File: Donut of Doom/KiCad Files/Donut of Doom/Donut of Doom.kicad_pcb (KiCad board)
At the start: 2 copper layers, 55.2 x 55.8 mm, 11 parts

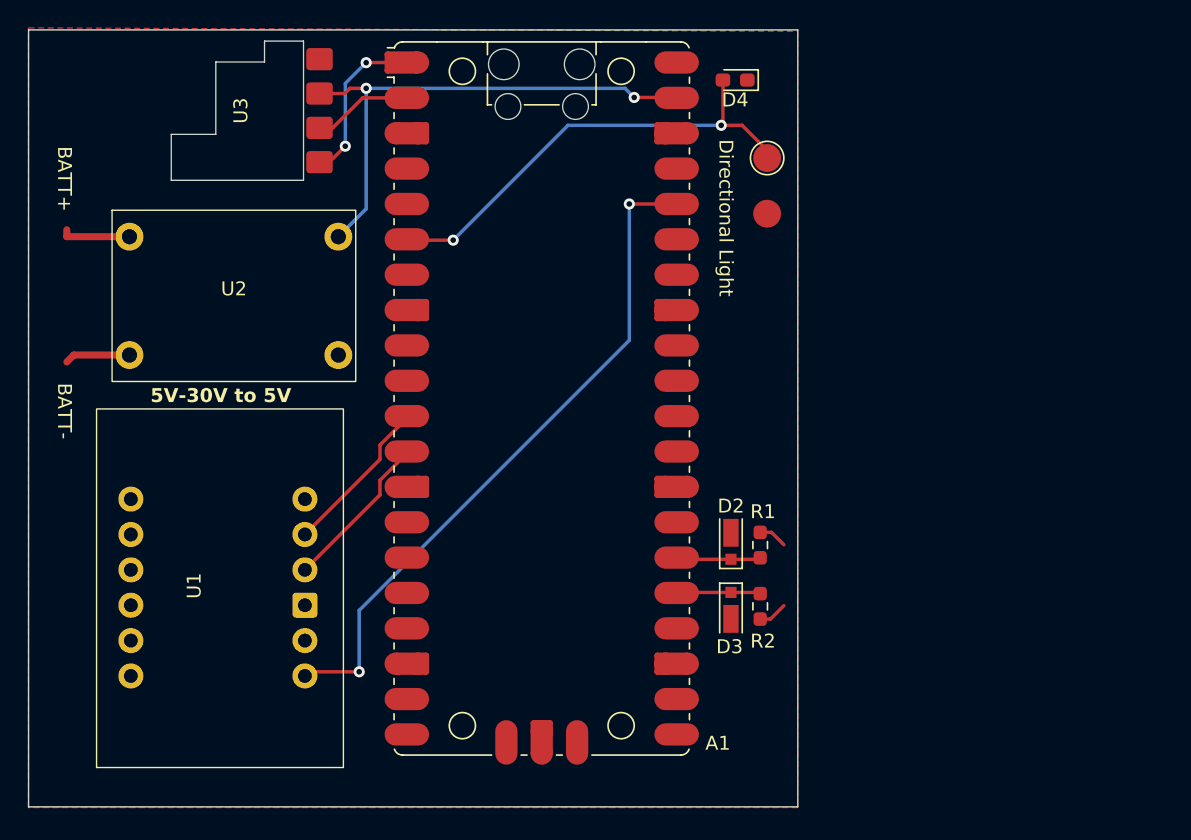
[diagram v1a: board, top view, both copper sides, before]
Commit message: New footprints for buck and accel, layout partially done.
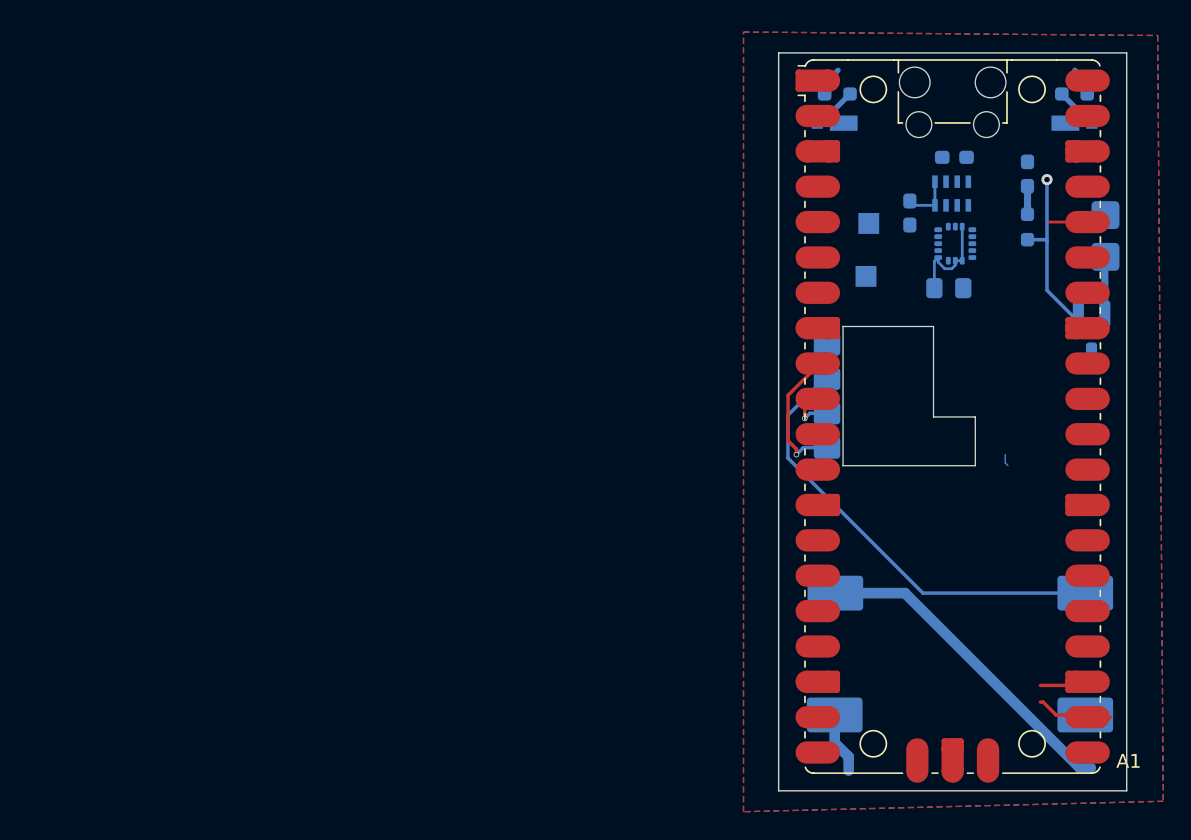
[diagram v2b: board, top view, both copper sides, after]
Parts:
- removed ?: , 
- removed the D4 at (135.0, 70.5)
- removed REF**: TestPoint_Pad_D2.0mm, TestPoint:TestPoint_Pad_D2.0mm
- removed the U1 at (91.6, 113.3)
- added 0.1uF1: 10uF, Capacitor_SMD:C_0603_1608Metric_Pad1.08x0.95mm_HandSolder, B.Cu at (147.6, 80.0)
- added C1: 10uF, Capacitor_SMD:C_0805_2012Metric_Pad1.18x1.45mm_HandSolder, B.Cu at (150.3, 85.5)
- added D1: RED 2V LED, Battlebots:2 pth Pads, B.Cu at (161.6, 81.7)
- added D2: RED 2V LED, LED_SMD:LED_0603_1608Metric_Pad1.05x0.95mm_HandSolder, B.Cu at (156.0, 77.3)
- added D6: GREEN ON LED, LED_SMD:LED_0603_1608Metric_Pad1.05x0.95mm_HandSolder, B.Cu at (150.8, 76.0)
- added Q1: Q_NMOS_GSD, Package_TO_SOT_SMD:SOT-23_Handsoldering, B.Cu at (160.6, 88.8)
- added R1: 100, Resistor_SMD:R_0603_1608Metric_Pad0.98x0.95mm_HandSolder, B.Cu at (156.0, 81.1)
- added RN1: R_Pack04_Split, Resistor_SMD:R_Array_Concave_4x0603, B.Cu at (150.6, 78.7)
- added TP1: INT1, TestPoint:TestPoint_Pad_1.5x1.5mm, B.Cu at (144.4, 84.6)
- added TP2: INT2, TestPoint:TestPoint_Pad_1.5x1.5mm, B.Cu at (144.6, 80.8)
- added U3: H3LIS331DLTR, Package_LGA:LGA-16_3x3mm_P0.5mm_LayoutBorder3x5y, B.Cu at (150.8, 82.2)
- D3, R2, U2: moved to B.Cu
- D4: renamed from D2; moved to B.Cu
- R3: renamed from R1; moved to B.Cu
- U1: renamed from U3; moved to B.Cu
- moved U2 58.1 mm to (151.2, 111.6)
- moved U1 51.0 mm to (146.8, 93.2)
- moved R3 39.5 mm to (159.4, 71.5), turned to 0 degrees
- moved D4 39.2 mm to (159.6, 73.6), turned to 180 degrees
- moved R2 37.2 mm to (142.3, 71.5), turned to 180 degrees
- moved D3 35.5 mm to (141.9, 73.6), turned to 0 degrees
- moved A1 29.5 mm to (150.6, 94.7)
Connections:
- A1 pad 1: Net-(A1-GPIO0) -> unconnected-(A1-GPIO0-Pad1)
- A1 pad 10: unconnected-(A1-GPIO7-Pad10) -> Net-(A1-GPIO7)
- A1 pad 2: Net-(A1-GPIO1) -> unconnected-(A1-GPIO1-Pad2)
- A1 pad 29: unconnected-(A1-GPIO22-Pad29) -> /Directional LED
- A1 pad 6: /GPIO4 -> unconnected-(A1-GPIO4-Pad6)
- A1 pad 9: unconnected-(A1-GPIO6-Pad9) -> Net-(A1-GPIO6)
- U1 pad 1: Net-(A1-GPIO0) -> Net-(A1-GPIO6)
- U1 pad 2: Net-(A1-GPIO1) -> Net-(A1-GPIO7)
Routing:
- net +3V3: track 48.3 -> 13.1 mm, vias 2 -> 0
- net /GPIO4: track 33.2 -> 0.00 mm, vias 2 -> 0
- net +BATT: track 5.00 -> 23.5 mm
- net Net-(A1-GPIO0): track 12.7 -> 0.00 mm, vias 2 -> 0
- net /Directional LED: track 0.00 -> 12.3 mm, vias 0 -> 1
- net /I2C0 SCL: track 12.2 -> 0.00 mm
- net /I2C0 SDA: track 12.2 -> 0.00 mm
- net Net-(A1-GPIO6): track 0.00 -> 10.6 mm, vias 0 -> 1
- net Net-(A1-GPIO1): track 7.96 -> 0.00 mm
- net unconnected-(A1-GPIO17-Pad22): track 0.00 -> 5.44 mm
- net /ESC2 PWM: track 6.89 -> 2.13 mm
- net +5V: track 36.8 -> 32.1 mm, vias 2 -> 0
- net Net-(A1-GPIO7): track 0.00 -> 4.45 mm, vias 0 -> 1
- net Net-(D1-A): track 0.00 -> 4.12 mm
- net /ESC1 PWM: track 6.85 -> 3.04 mm
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- added copper zone on B.Cu, net GND
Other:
- board size 55.2 x 55.8 mm -> 25 x 53 mm
- board text removed: "Directional Light"

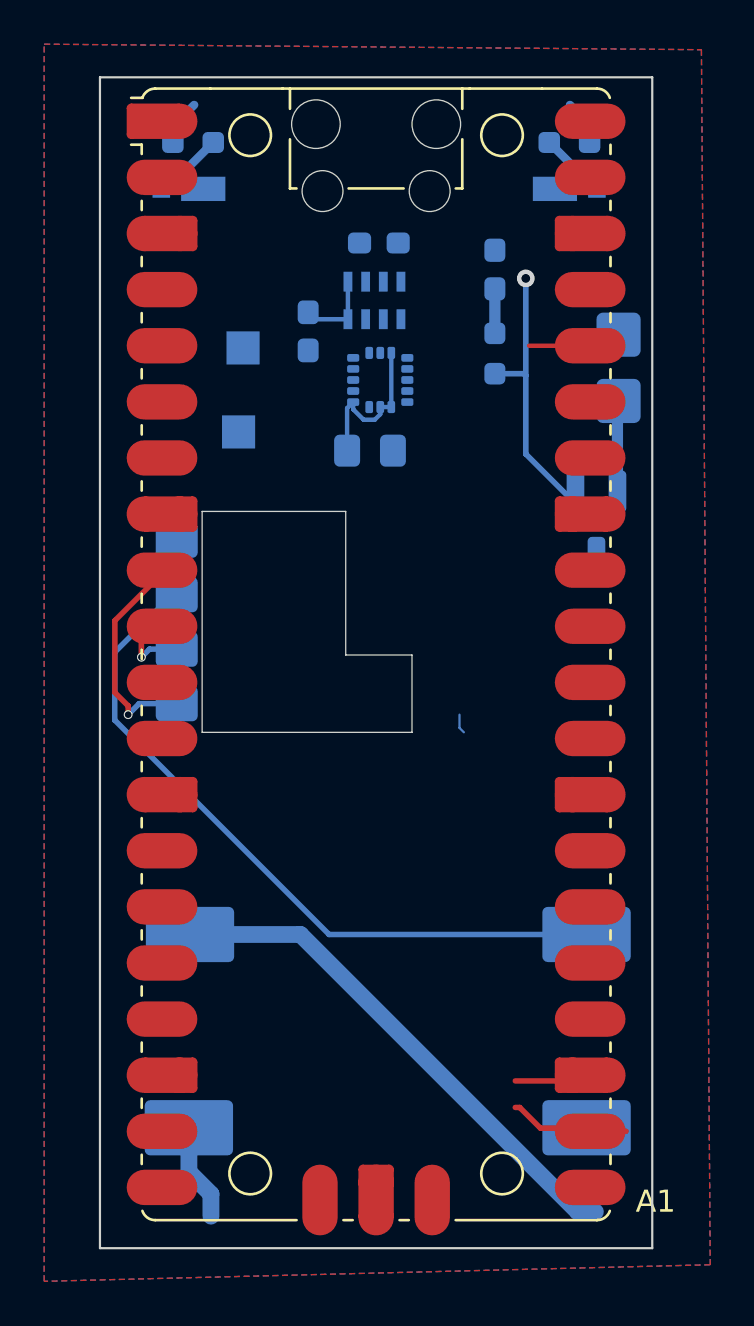
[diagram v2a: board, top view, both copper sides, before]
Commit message: PCB almost finalized, awaiting dfm
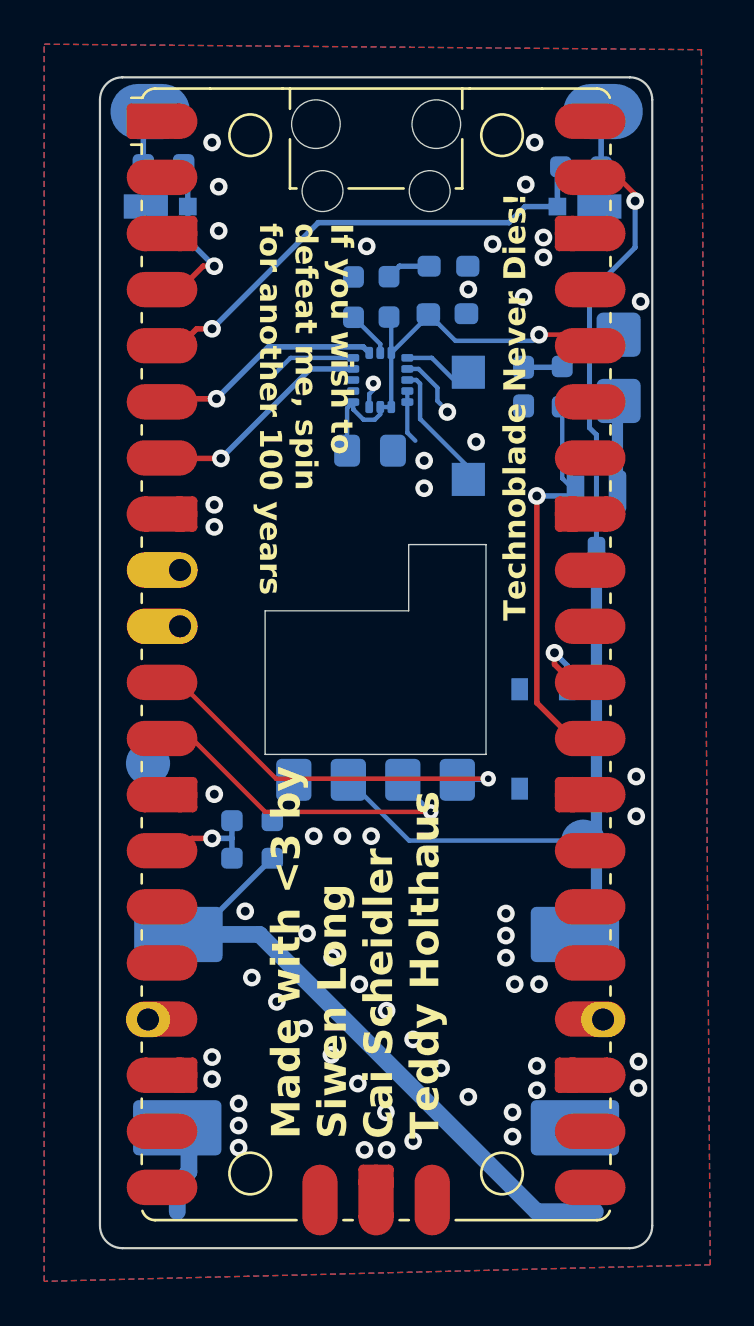
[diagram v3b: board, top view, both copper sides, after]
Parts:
- removed RN1: R_Pack04_Split, Resistor_SMD:R_Array_Concave_4x0603
- added ?: , , F.Cu at (140.3, 111.2)
- added ?: , , B.Cu at (141.8, 93.4)
- added ?: , , B.Cu at (141.8, 90.8)
- added ?: , , B.Cu at (160.9, 111.2)
- added G***: LOGO, LOGO, B.Cu at (143.0, 79.8)
- added G***: LOGO, LOGO, B.Cu at (145.8, 85.8)
- added PWM1: ~, Battlebots:Oval Pad, B.Cu at (140.4, 70.1)
- added PWM2: ~, Battlebots:Oval Pad, B.Cu at (160.9, 70.1)
- added R4: 10k, Resistor_SMD:R_0603_1608Metric_Pad0.98x0.95mm_HandSolder, B.Cu at (149.6, 78.5)
- added R5: 10k, Resistor_SMD:R_0603_1608Metric_Pad0.98x0.95mm_HandSolder, B.Cu at (151.2, 78.5)
- added R6: 300, Resistor_SMD:R_0603_1608Metric_Pad0.98x0.95mm_HandSolder, B.Cu at (145.0, 103.9)
- added R7: 100, Resistor_SMD:R_0603_1608Metric_Pad0.98x0.95mm_HandSolder, B.Cu at (145.0, 102.2)
- added S1: TL3365AF180QG, TL3365AF180QG:SW_TL3365AF180QG, B.Cu at (158.2, 98.5)
- added TP3: +5V, TestPoint:TestPoint_Pad_D2.0mm, B.Cu at (160.0, 103.2)
- added TP4: GND, TestPoint:TestPoint_Pad_D2.0mm, B.Cu at (140.3, 99.6)
- C2: renamed from 0.1uF1; value 10uF -> 0.1uF
- moved TP1 10.6 mm to (154.8, 86.8)
- moved TP2 10.3 mm to (154.8, 81.9)
- moved C2 6.35 mm to (153.8, 79.2), turned to 0 degrees
- moved D2 5.45 mm to (157.3, 82.5), turned to 90 degrees
- moved U1 4.34 mm to (150.6, 95.2), turned to 180 degrees
- moved R1 3.40 mm to (159.1, 82.5)
- moved D5 3.32 mm to (153.9, 77.1), turned to 180 degrees
- moved R2 1.67 mm to (141.0, 72.5)
- moved R3 1.22 mm to (159.9, 72.6)
- moved D3 1.16 mm to (141.1, 74.4), turned to 180 degrees
- moved D4 0.84 mm to (159.8, 74.4), turned to 0 degrees
- moved U2 0.53 mm to (150.6, 111.6)
- renumbered D6 to D5
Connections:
- A1 pad 10: Net-(A1-GPIO7) -> unconnected-(A1-GPIO7-Pad10)
- A1 pad 11: /I2C0 SDA -> Net-(A1-GPIO8)
- A1 pad 12: /I2C0 SCL -> Net-(A1-GPIO9)
- A1 pad 14: unconnected-(A1-GPIO10-Pad14) -> /BATTV
- A1 pad 25: /ESC1 PWM -> unconnected-(A1-GPIO19-Pad25)
- A1 pad 26: /ESC2 PWM -> unconnected-(A1-GPIO20-Pad26)
- A1 pad 30: unconnected-(A1-RUN-Pad30) -> Net-(A1-RUN)
- A1 pad 4: unconnected-(A1-GPIO2-Pad4) -> /ESC1
- A1 pad 5: unconnected-(A1-GPIO3-Pad5) -> /ESC2
- A1 pad 6: unconnected-(A1-GPIO4-Pad6) -> /I2C0 SDA
- A1 pad 7: unconnected-(A1-GPIO5-Pad7) -> /I2C0 SCL
- A1 pad 9: Net-(A1-GPIO6) -> unconnected-(A1-GPIO6-Pad9)
- D3 pad 1: /ESC1 PWM -> /ESC1
- D4 pad 1: /ESC2 PWM -> /ESC2
- R2 pad 1: /ESC1 PWM -> /ESC1
- R3 pad 1: /ESC2 PWM -> /ESC2
- U1 pad 1: Net-(A1-GPIO6) -> Net-(A1-GPIO8)
- U1 pad 2: Net-(A1-GPIO7) -> Net-(A1-GPIO9)
- U2 pad 2: -BATT -> GND
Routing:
- net /ESC2: track 0.00 -> 21.6 mm, vias 0 -> 1
- net +5V: track 32.1 -> 50.2 mm, vias 0 -> 1
- net Net-(A1-GPIO8): track 0.00 -> 17.2 mm, vias 0 -> 1
- net Net-(A1-GPIO9): track 0.00 -> 14.7 mm, vias 0 -> 1
- net GND: track 2.94 -> 14.7 mm, vias 0 -> 58
- net Net-(A1-GPIO6): track 10.6 -> 0.00 mm, vias 1 -> 0
- net /I2C0 SDA: track 0.00 -> 9.72 mm, vias 0 -> 1
- net /I2C0 SCL: track 0.00 -> 9.62 mm, vias 0 -> 1
- net /ESC1: track 0.00 -> 7.18 mm, vias 0 -> 1
- net Net-(U3-INT1): track 0.00 -> 6.03 mm
- net +BATT: track 23.5 -> 29.2 mm
- net unconnected-(A1-GPIO17-Pad22): track 5.44 -> 0.00 mm
- net +3V3: track 13.1 -> 18.5 mm, vias 0 -> 1
- net /Directional LED: track 12.3 -> 17.6 mm
- net Net-(A1-GPIO7): track 4.45 -> 0.00 mm, vias 1 -> 0
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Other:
- outline, holes or cut-outs redrawn
- board text added: "+"
- board text added: "+5V"
- board text added: "-"
- board text added: "5V"
- board text added: "5VLED"
- board text added: ":3"
- board text added: "BATT"
- board text added: "BATT SENSE"
- board text added: "ELRS Reciever"
- board text added: "GND"
- board text added: "INT1"
- board text added: "INT2"
- board text added: "If you wish to defeat me, spin for another 100 years"
- board text added: "Made with <3 by Siwen Long Cai Scheidler Teddy Holthaus"
- board text added: "P10"
- board text added: "P17"
- board text added: "P24"
- board text added: "P9"
- board text added: "PCB V1 Donut of Doom"
- board text added: "Technoblade Never Dies!"
- board text added: "X"
- board text added: "Y"

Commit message: Finalized V1 Order, DFM completed
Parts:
- added G***: LOGO, LOGO, F.Cu at (152.8, 82.0)
- added TP5: +BATT, Battlebots:3.5mmx2.5mm_oval_smd_pad, B.Cu at (159.8, 119.9)
- added TP6: -BATT, Battlebots:3.5mmx2.5mm_oval_smd_pad, B.Cu at (141.6, 119.9)
- TP4: footprint TestPoint:TestPoint_Pad_D2.0mm -> TestPoint:TestPoint_Pad_D3.0mm
- moved D1 1.25 mm to (161.6, 83.0)
- renumbered PWM1 to ESC1, PWM2 to ESC2
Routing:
- net Net-(D1-A): track 4.12 -> 2.87 mm
- net GND: vias 58 -> 69
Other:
- board text added: "BATT-> SENSE"
- board text added: "Reset>"
- board text removed: "+5V"
- board text removed: "BATT SENSE"

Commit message: fixed resistor values
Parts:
- R5: value 10k -> 100
- moved PWM2 0.29 mm to (160.8, 70.3)
- moved PWM1 0.25 mm to (140.4, 70.3)
- renumbered ESC1 to PWM1, ESC2 to PWM2
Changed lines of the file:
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@@
 	)
 	(setup
+		(stackup
+			(layer "F.SilkS"
+				(type "Top Silk Screen")
+			)
+			(layer "F.Paste"
+				(type "Top Solder Paste")
+			)
+			(layer "F.Mask"
+				(type "Top Solder Mask")
+				(thickness 0.01)
+			)
+			(layer "F.Cu"
+				(type "copper")
+				(thickness 0.035)
+			)
+			(layer "dielectric 1"
+				(type "core")
+				(thickness 1.51)
+				(material "FR4")
+				(epsilon_r 4.5)
+				(loss_tangent 0.02)
+			)
+			(layer "B.Cu"
+				(type "copper")
+				(thickness 0.035)
+			)
+			(layer "B.Mask"
+				(type "Bottom Solder Mask")
+				(thickness 0.01)
+			)
+			(layer "B.Paste"
+				(type "Bottom Solder Paste")
+			)
+			(layer "B.SilkS"
+				(type "Bottom Silk Screen")
+			)
+			(copper_finish "None")
+			(dielectric_constraints no)
+		)
 		(pad_to_mask_clearance 0)
 		(allow_soldermask_bridges_in_footprints no)
@@
 		(tags "capacitor handsolder")
 		(property "Reference" "C2"
-			(at 2.45 0 0)
+			(at 2.65 0.4 0)
 			(layer "B.SilkS")
 			(effects
 				(font
-					(size 0.7 0.7)
+					(size 1 1)
 					(thickness 0.15)
 					(bold yes)
@@
 	(footprint "Battlebots:Oval Pad"
 		(layer "B.Cu")
-		(at 160.9 70.1 180)
-		(property "Reference" "ESC2"
+		(at 160.75 70.35 180)
+		(property "Reference" "PWM2"
 			(at 4.1 -0.2 0)
 			(unlocked yes)
@@
 			)
 		)
-		(property "Value" "10k"
+		(property "Value" "100"
 			(at 0 -1.43 90)
 			(layer "B.Fab")
@@
 	(footprint "Battlebots:Oval Pad"
 		(layer "B.Cu")
-		(at 140.4 70.1 180)
-		(property "Reference" "ESC1"
+		(at 140.4 70.35 180)
+		(property "Reference" "PWM1"
 			(at -4 -0.2 0)
 			(unlocked yes)
@@
 	)
 	(via
-		(at 144.9 94.85)
+		(at 144.7 94.85)
 		(size 0.8)
 		(drill 0.4)
@@
 	)
 	(via
-		(at 162.35 79.4)
+		(at 162.3 79.4)
 		(size 0.8)
 		(drill 0.4)
@@
 	)
 	(via
-		(at 162.4 102)
+		(at 162.3 102)
 		(size 0.8)
 		(drill 0.4)
@@
 	)
 	(via
-		(at 162.4 100.2)
+		(at 162.3 99.85)
 		(size 0.8)
 		(drill 0.4)
@@
 	)
 	(via
-		(at 144.9 96)
+		(at 144.7 96)
 		(size 0.8)
 		(drill 0.4)
@@
 	)
 	(segment
-		(start 162.35 73.85)
-		(end 161.58 73.08)
+		(start 162.25 76.6)
+		(end 162.35 76.5)
 		(width 0.2286)
 		(layer "F.Cu")
@@
 	)
 	(segment
-		(start 162.35 74.15)
+		(start 162.35 76.5)
 		(end 162.35 73.85)
 		(width 0.2286)
@@
 		(net 11)
 	)
+	(segment
+		(start 162.35 73.85)
+		(end 161.58 73.08)
+		(width 0.2286)
+		(layer "F.Cu")
+		(net 11)
+	)
 	(via
-		(at 162.35 74.15)
+		(at 162.25 76.6)
 		(size 0.8)
 		(drill 0.4)
@@
 	)
 	(segment
-		(start 160.2847 85.6347)
-		(end 160.6 85.95)
+		(start 162 76.6)
+		(end 160.2847 78.3153)
 		(width 0.2286)
 		(layer "B.Cu")
@@
 	)
 	(segment
-		(start 162.35 74.15)
-		(end 162.35 76.25)
-		(width 0.2286)
+		(start 160.6 103.1)
+		(end 160.6 106.9)
+		(width 0.508)
 		(layer "B.Cu")
 		(net 11)
 	)
 	(segment
-		(start 162.35 76.25)
-		(end 160.2847 78.3153)
+		(start 160.2847 85.6347)
+		(end 160.6 85.95)
 		(width 0.2286)
 		(layer "B.Cu")
@@
 	)
 	(segment
-		(start 160.6 103.1)
-		(end 160.6 106.9)
-		(width 0.508)
+		(start 152.116667 103.1)
+		(end 160.6 103.1)
+		(width 0.2032)
 		(layer "B.Cu")
 		(net 11)
 	)
 	(segment
-		(start 152.116667 103.1)
-		(end 160.6 103.1)
-		(width 0.2032)
+		(start 160.2847 78.3153)
+		(end 160.2847 85.6347)
+		(width 0.2286)
 		(layer "B.Cu")
 		(net 11)
@@
 	)
 	(segment
-		(start 160.2847 78.3153)
-		(end 160.2847 85.6347)
+		(start 162.25 76.6)
+		(end 162 76.6)
 		(width 0.2286)
 		(layer "B.Cu")
